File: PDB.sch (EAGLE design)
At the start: 60 parts, among them IC1 LM555N

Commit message: created PDB board
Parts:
- renumbered ADD_SWITCH to ADD2_SWITCH
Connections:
- new net VDD_ADD1: C9.1, R8.1
- new net VDD_ADD2: C8.1, R7.1
- new net VDD_W: C10.1, D1.C, R9.1
- net VDD: no longer C10.1, C8.1, C9.1, D1.C, R7.1, R8.1, R9.1
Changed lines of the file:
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@@
 <part name="R10" library="rcl" library_urn="urn:adsk.eagle:library:334" deviceset="R-US_" device="R0805" package3d_urn="urn:adsk.eagle:package:23553/2" value="1K"/>
 <part name="R11" library="rcl" library_urn="urn:adsk.eagle:library:334" deviceset="R-US_" device="R0805" package3d_urn="urn:adsk.eagle:package:23553/2" value="10K"/>
-<part name="ADD_SWITCH" library="switch" library_urn="urn:adsk.eagle:library:380" deviceset="M9040P" device="" package3d_urn="urn:adsk.eagle:package:27676/1"/>
+<part name="ADD2_SWITCH" library="switch" library_urn="urn:adsk.eagle:library:380" deviceset="M9040P" device="" package3d_urn="urn:adsk.eagle:package:27676/1"/>
 <part name="ADD1_SWITCH" library="switch" library_urn="urn:adsk.eagle:library:380" deviceset="M9040P" device="" package3d_urn="urn:adsk.eagle:package:27676/1"/>
 <part name="WIPER_SWITCH" library="switch" library_urn="urn:adsk.eagle:library:380" deviceset="M9040P" device="" package3d_urn="urn:adsk.eagle:package:27676/1"/>
@@
 <instance part="R10" gate="G$1" x="48.26" y="88.9" rot="R270"/>
 <instance part="R11" gate="G$1" x="58.42" y="93.98" rot="R270"/>
-<instance part="ADD_SWITCH" gate="1" x="-66.04" y="-30.48" rot="R270"/>
+<instance part="ADD2_SWITCH" gate="1" x="-66.04" y="-30.48" rot="R270"/>
 <instance part="ADD1_SWITCH" gate="1" x="-27.94" y="-33.02" rot="R270"/>
 <instance part="WIPER_SWITCH" gate="1" x="12.7" y="-33.02" rot="R270"/>
@@
 </segment>
 <segment>
-<pinref part="SUPPLY19" gate="G$1" pin="VDD"/>
-<wire x1="-58.42" y1="60.96" x2="-58.42" y2="55.88" width="0.1524" layer="91"/>
-<pinref part="C8" gate="G$1" pin="1"/>
-<junction x="-58.42" y="55.88"/>
-<pinref part="R7" gate="G$1" pin="1"/>
-<wire x1="-58.42" y1="48.26" x2="-58.42" y2="55.88" width="0.1524" layer="91"/>
-</segment>
-<segment>
-<pinref part="SUPPLY11" gate="G$1" pin="VDD"/>
-<wire x1="-27.94" y1="60.96" x2="-27.94" y2="55.88" width="0.1524" layer="91"/>
-<pinref part="C9" gate="G$1" pin="1"/>
-<junction x="-27.94" y="55.88"/>
-<pinref part="R8" gate="G$1" pin="1"/>
-<wire x1="-27.94" y1="48.26" x2="-27.94" y2="55.88" width="0.1524" layer="91"/>
-</segment>
-<segment>
-<pinref part="SUPPLY29" gate="G$1" pin="VDD"/>
-<wire x1="17.78" y1="66.04" x2="17.78" y2="60.96" width="0.1524" layer="91"/>
-<pinref part="C10" gate="G$1" pin="1"/>
-<junction x="17.78" y="60.96"/>
-<pinref part="R9" gate="G$1" pin="1"/>
-<wire x1="17.78" y1="45.72" x2="17.78" y2="50.8" width="0.1524" layer="91"/>
-<pinref part="D1" gate="G$1" pin="C"/>
-<wire x1="17.78" y1="50.8" x2="17.78" y2="60.96" width="0.1524" layer="91"/>
-<junction x="17.78" y="50.8"/>
-<label x="12.7" y="63.5" size="1.778" layer="95"/>
-</segment>
-<segment>
 <pinref part="SUPPLY31" gate="G$1" pin="VDD"/>
 <pinref part="ADD2_OUT3" gate="G$1" pin="V+"/>
@@
 </segment>
 <segment>
-<pinref part="ADD_SWITCH" gate="1" pin="P"/>
+<pinref part="ADD2_SWITCH" gate="1" pin="P"/>
 <wire x1="-71.12" y1="-33.02" x2="-73.66" y2="-33.02" width="0.1524" layer="91"/>
 <pinref part="SUPPLY5" gate="G$1" pin="VDD"/>
@@
 <net name="H6" class="0">
 <segment>
-<pinref part="ADD_SWITCH" gate="1" pin="O"/>
+<pinref part="ADD2_SWITCH" gate="1" pin="O"/>
 <wire x1="-60.96" y1="-30.48" x2="-58.42" y2="-30.48" width="0.1524" layer="91"/>
 <label x="-58.42" y="-30.48" size="1.778" layer="95" xref="yes"/>
@@
 </segment>
 </net>
+<net name="VDD_W" class="0">
+<segment>
+<pinref part="SUPPLY29" gate="G$1" pin="VDD"/>
+<wire x1="17.78" y1="66.04" x2="17.78" y2="60.96" width="0.1524" layer="91"/>
+<pinref part="C10" gate="G$1" pin="1"/>
+<junction x="17.78" y="60.96"/>
+<pinref part="R9" gate="G$1" pin="1"/>
+<wire x1="17.78" y1="45.72" x2="17.78" y2="50.8" width="0.1524" layer="91"/>
+<pinref part="D1" gate="G$1" pin="C"/>
+<wire x1="17.78" y1="50.8" x2="17.78" y2="60.96" width="0.1524" layer="91"/>
+<junction x="17.78" y="50.8"/>
+<label x="15.24" y="53.34" size="1.778" layer="95" rot="R90"/>
+</segment>
+</net>
+<net name="VDD_ADD1" class="0">
+<segment>
+<pinref part="SUPPLY11" gate="G$1" pin="VDD"/>
+<wire x1="-27.94" y1="60.96" x2="-27.94" y2="55.88" width="0.1524" layer="91"/>
+<pinref part="C9" gate="G$1" pin="1"/>
+<junction x="-27.94" y="55.88"/>
+<pinref part="R8" gate="G$1" pin="1"/>
+<wire x1="-27.94" y1="48.26" x2="-27.94" y2="55.88" width="0.1524" layer="91"/>
+<label x="-30.48" y="48.26" size="1.778" layer="95" rot="R90"/>
+</segment>
+</net>
+<net name="VDD_ADD2" class="0">
+<segment>
+<pinref part="SUPPLY19" gate="G$1" pin="VDD"/>
+<wire x1="-58.42" y1="60.96" x2="-58.42" y2="55.88" width="0.1524" layer="91"/>
+<pinref part="C8" gate="G$1" pin="1"/>
+<junction x="-58.42" y="55.88"/>
+<pinref part="R7" gate="G$1" pin="1"/>
+<wire x1="-58.42" y1="48.26" x2="-58.42" y2="55.88" width="0.1524" layer="91"/>
+<label x="-60.96" y="48.26" size="1.778" layer="95" rot="R90"/>
+</segment>
+</net>

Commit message: updated board layout
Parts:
- removed ADD2_OUT1, ADD2_OUT2, ADD2_OUT3, ADD2_OUT4, ADD2_OUT5, ADD2_OUT6, ADD2_OUT7: POWERPOLE_POWER25A, powerpoles:POWERPOLE_POWER25A
- removed DAY_SWITCH: (no value), switch:M9040P
- added ADD1_OUT, BRAKE_OUT, HAZL_OUT, HAZR_OUT, HEADLIGHTS_OUT, REARLIGHTS_OUT, VDD_IN1, WIPER_OUT: POWERPOLE_POWER25A_HORIZONTAL_G2, powerpoles:POWERPOLE_POWER25A_HORIZONTAL_G2
- added HEADLIGHTS, REARLIGHTS: (no value), switch:M9040P
- ADD2_OUT, VDD_IN: value POWERPOLE_POWER25A -> POWERPOLE_POWER25A_HORIZONTAL_G2; device powerpoles:POWERPOLE_POWER25A -> powerpoles:POWERPOLE_POWER25A_HORIZONTAL_G2
- renumbered BRAKE_SENSOR to BRAKE_SNS_OVR
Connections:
- new net H8: HEADLIGHTS.O, R18.1
- net GND: now also VDD_IN1.GND
- net H1: now also VDD_IN1.V+
- net H7: now also REARLIGHTS.O; no longer DAY_SWITCH.O, R18.1
- net N$1: now also HEADLIGHTS_OUT.GND; no longer ADD2_OUT6.GND
- net N$17: now also ADD1_OUT.GND; no longer ADD2_OUT1.GND
- net N$18: now also ADD1_OUT.V+; no longer ADD2_OUT1.V+
- net N$19: now also WIPER_OUT.GND; no longer ADD2_OUT2.GND
- net N$20: now also WIPER_OUT.V+; no longer ADD2_OUT2.V+
- net N$21: now also HAZL_OUT.GND; no longer ADD2_OUT3.GND
- net N$23: now also HAZR_OUT.GND; no longer ADD2_OUT4.GND
- net N$25: now also BRAKE_OUT.GND; no longer ADD2_OUT5.GND
- net N$3: now also REARLIGHTS_OUT.GND; no longer ADD2_OUT7.GND
- net VDD: now also BRAKE_OUT.V+, HAZL_OUT.V+, HAZR_OUT.V+, HEADLIGHTS.P, HEADLIGHTS_OUT.V+, REARLIGHTS.P, REARLIGHTS_OUT.V+; no longer ADD2_OUT3.V+, ADD2_OUT4.V+, ADD2_OUT5.V+, ADD2_OUT6.V+, ADD2_OUT7.V+, DAY_SWITCH.P
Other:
- moved on the sheet: ADD1_SWITCH

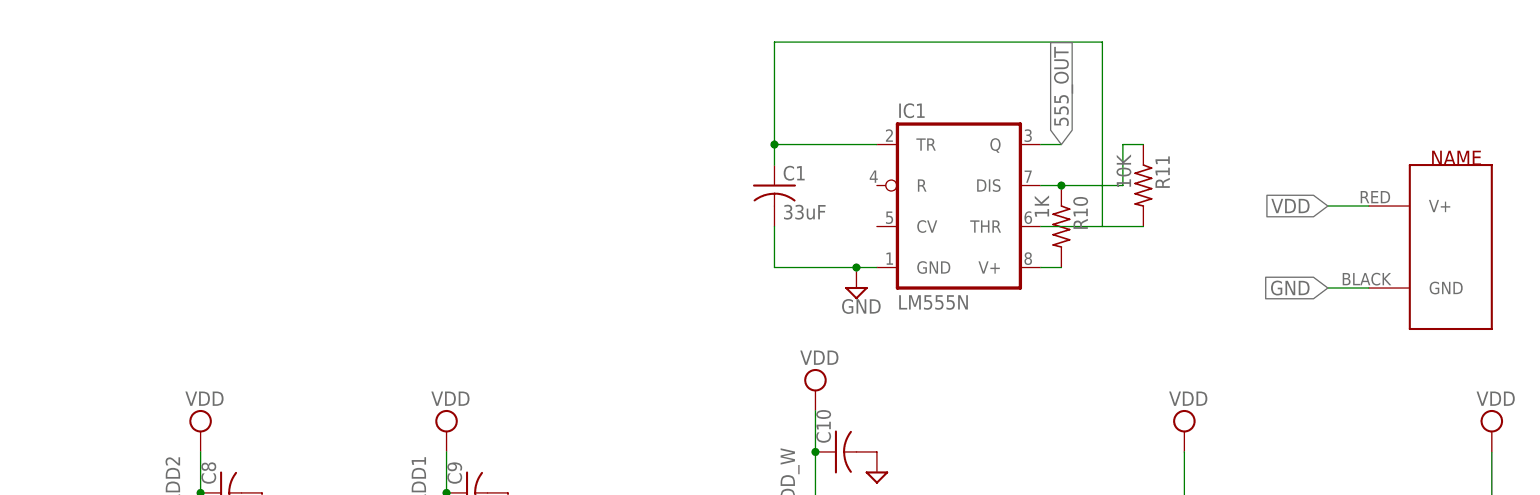
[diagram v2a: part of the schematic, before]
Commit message: added trim pot
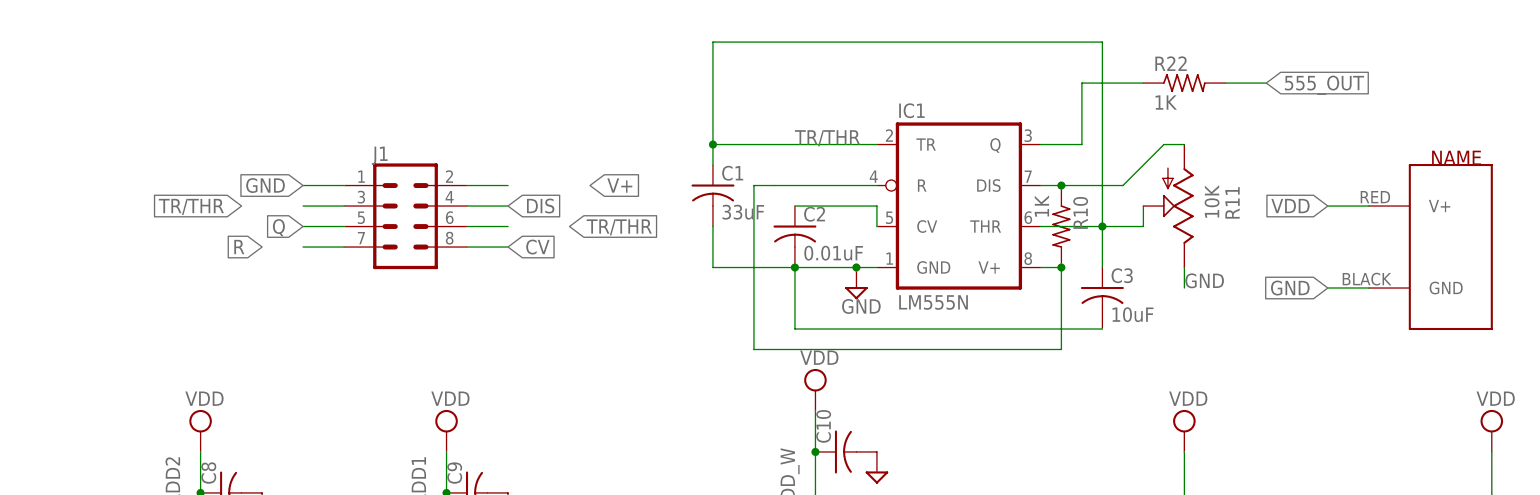
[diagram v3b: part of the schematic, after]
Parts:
- added C2: 0.01uF, rcl:C-USC0805
- added C3: 10uF, rcl:C-USC0805K
- added J1: (no value), SparkFun-Connectors:CONN_04X2
- added R22: 1K, rcl:R-US_R0805
- R11: device rcl:R-US_R0805 -> pot:TRIM_US-B25U
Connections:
- removed net N$4: C1.1, IC1.THR, IC1.TR, R11.2
- removed net N$5: IC1.DIS, R10.1, R11.1
- removed net N$6: IC1.V+, R10.2
- new net CV: C2.1, IC1.CV, J1.8
- new net DIS: IC1.DIS, J1.4, R10.1, R11.A
- new net Q: IC1.Q, J1.5, R22.1
- new net R: IC1.R, IC1.V+, J1.7, R10.2
- new net TR/THR: C1.1, C3.1, IC1.THR, IC1.TR, J1.3, J1.6, R11.S
- new net V+: J1.2
- net 555_OUT: now also R22.2; no longer IC1.Q
- net GND: now also C2.2, C3.2, J1.1, R11.E
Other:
- moved on the sheet: C1

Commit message: changed PDB
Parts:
- removed IC1: LM555N, linear:LM555N
- removed J1: (no value), SparkFun-Connectors:CONN_04X2
- added J2, J3: (no value), SparkFun-Connectors:CONN_04LONGPADS
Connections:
- removed net R: IC1.R, IC1.V+, J1.7, R10.2
- net CV: now also J3.3; no longer IC1.CV, J1.8
- net DIS: now also J2.3; no longer IC1.DIS, J1.4
- net GND: now also J3.4; no longer IC1.GND, J1.1
- net Q: now also J2.4; no longer IC1.Q, J1.5
- net TR/THR: now also J2.2, J3.1; no longer IC1.THR, IC1.TR, J1.3, J1.6
- net V+: now also J2.1, J3.2, R10.2; no longer J1.2
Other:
- note added: "12V IN"
- note added: "555 Timer"
- note added: "BRAKE_SNS"
- note added: "Switches"
- moved on the sheet: ADD2_SWITCH, C1, C10, C2, C3, D1, D2, R10, R11, R14, R22, R3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

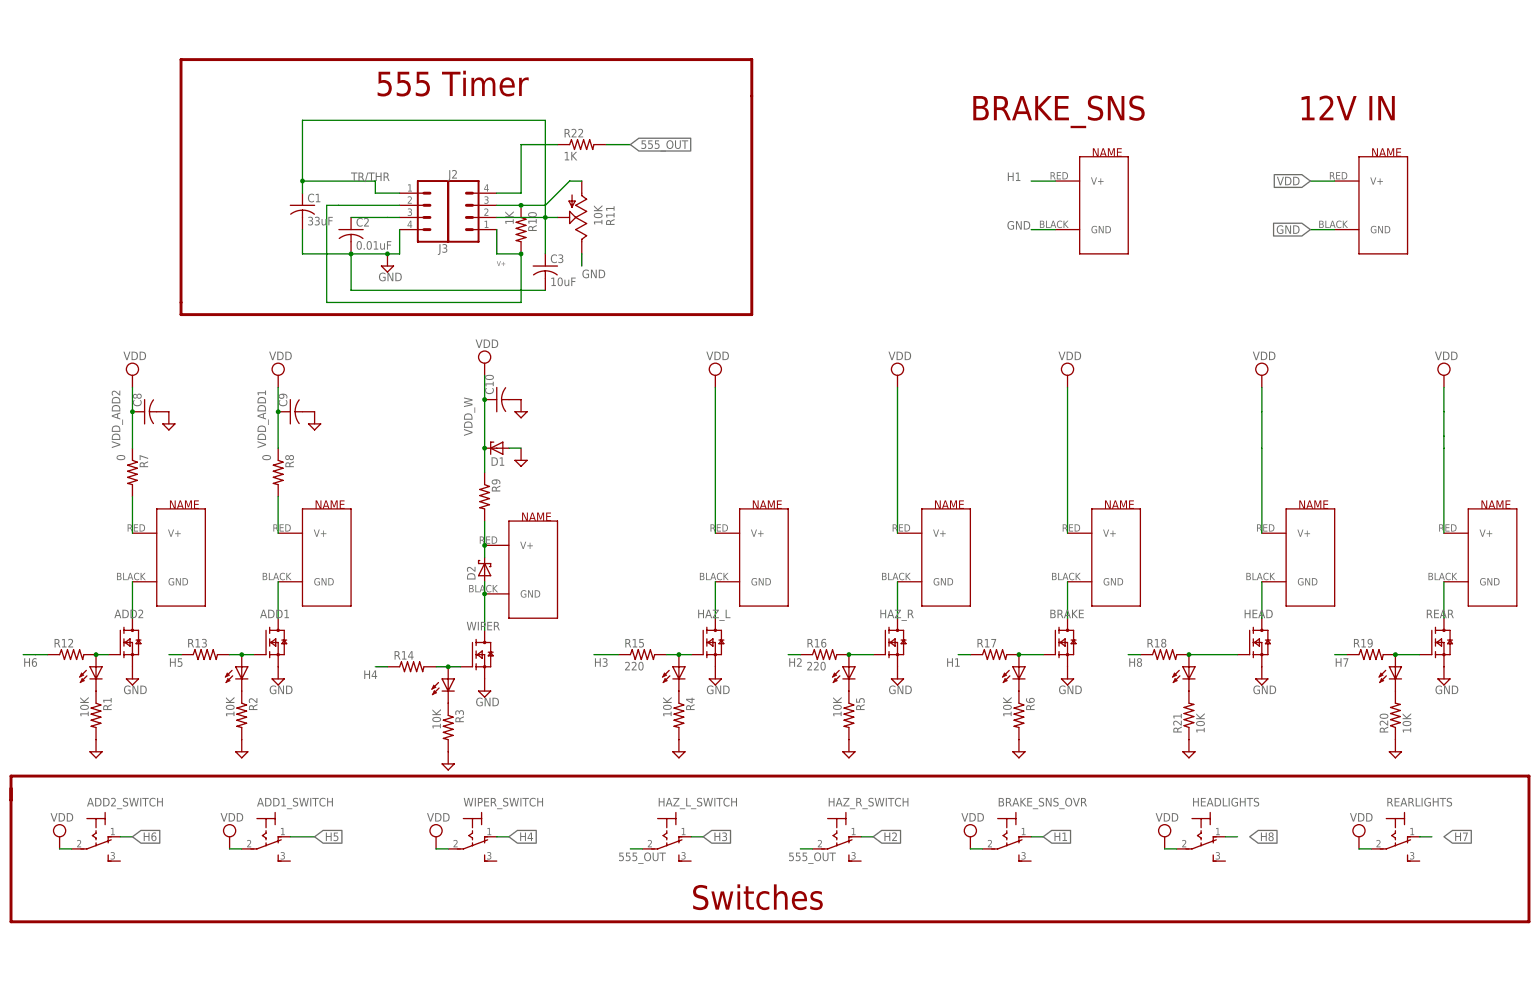
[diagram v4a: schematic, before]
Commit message: improved layout of 555 timer
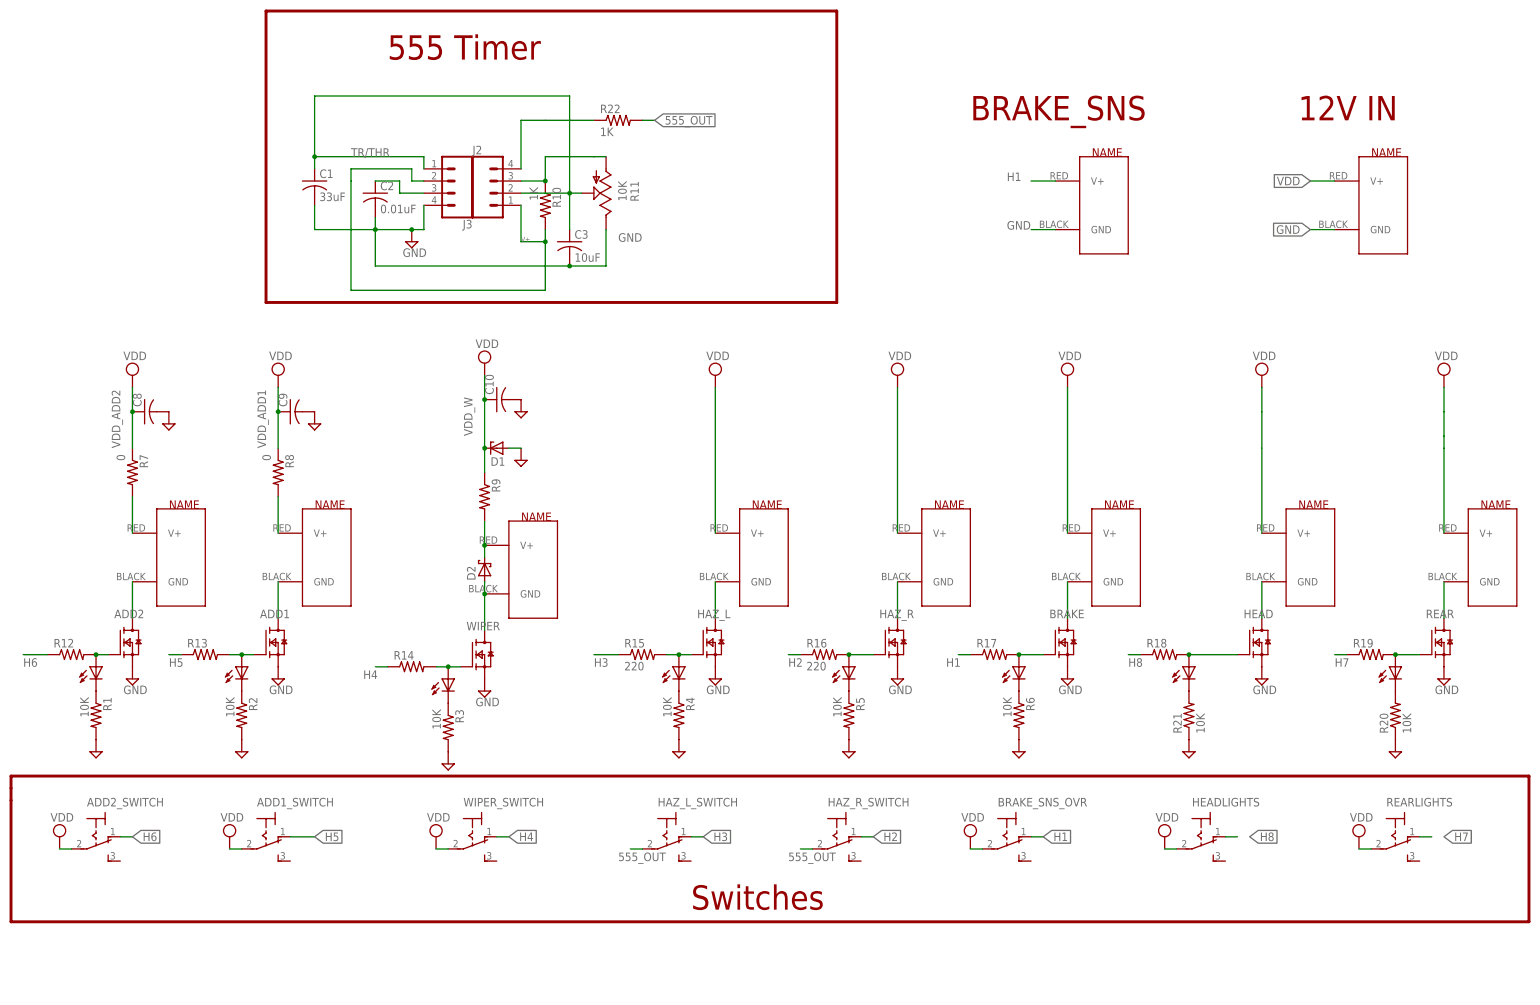
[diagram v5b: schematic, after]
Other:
- moved on the sheet: C1, C2, C3, J2, J3, R10, R11, R22
